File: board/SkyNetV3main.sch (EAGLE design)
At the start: 61 parts, among them IC1 HC_05, IC2 RF4463PRO, IC3 LPC1768, IC4 BCX17, IC5 TPS63001, IC6 MCP73871-2CCI/ML, Q1 32.768KHz, Q2 12MHz, Q3 IRLM6402, Q4 BSS138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

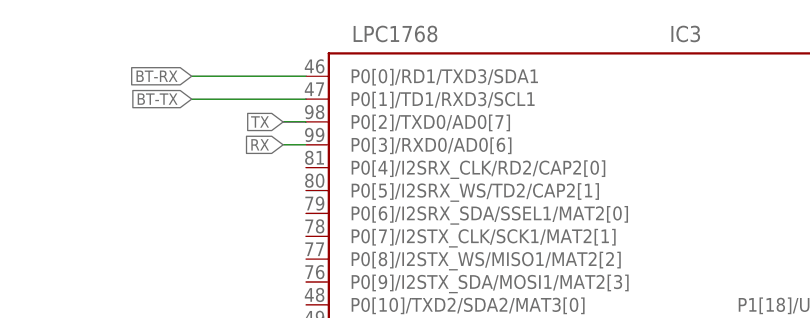
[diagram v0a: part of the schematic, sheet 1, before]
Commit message: corrected some distance problems and missing VALUEs
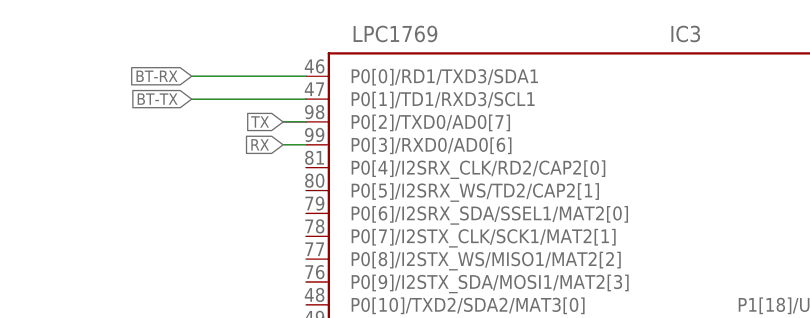
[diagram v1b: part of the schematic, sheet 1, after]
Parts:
- IC3: value LPC1768 -> LPC1769
- JP4: value (none) -> EXT
- SJ1: value (none) -> MEASURE
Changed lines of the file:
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@@
 </classes>
 <parts>
-<part name="IC3" library="lpc1xxx-v6" deviceset="LPC1768" device=""/>
+<part name="IC3" library="lpc1xxx-v6" deviceset="LPC1768" device="" value="LPC1769"/>
 <part name="IC1" library="Bluetooth HC-05" deviceset="HC_05" device=""/>
 <part name="FRAME1" library="frames" deviceset="A4L-LOC" device="" value="SkyNet Main"/>
@@
 <part name="GND31" library="supply1" deviceset="GND" device=""/>
 <part name="LED2" library="adafruit" deviceset="RGBLED" device="5050"/>
-<part name="SJ1" library="jumper" deviceset="SJ" device=""/>
+<part name="SJ1" library="jumper" deviceset="SJ" device="" value="MEASURE"/>
 <part name="SJ2" library="jumper" deviceset="SJ" device="" value="PROG"/>
 <part name="C12" library="microbuilder" deviceset="CAP_TANTALUM" device="C/6032_WAVE" value="100u"/>
@@
 <part name="GND19" library="supply1" deviceset="GND" device=""/>
 <part name="GND21" library="supply1" deviceset="GND" device=""/>
-<part name="JP4" library="skynet_other" deviceset="PIN-HEAD-1X3" device=""/>
+<part name="JP4" library="skynet_other" deviceset="PIN-HEAD-1X3" device="" value="EXT"/>
 <part name="FRAME4" library="frames" deviceset="A4L-LOC" device="" value="SkyNet Main"/>
 </parts>

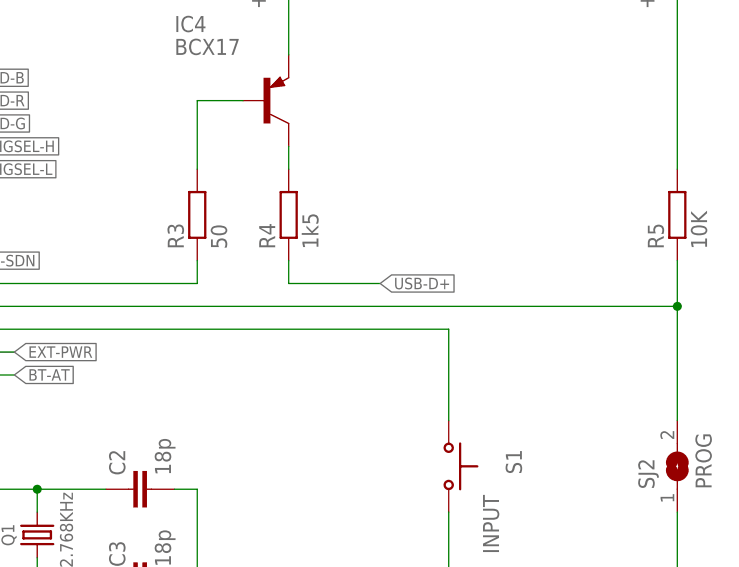
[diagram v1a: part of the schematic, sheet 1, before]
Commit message: layout & schematic fixes
+ layout: better ground flow
+ layout: more space for single parts
+ layout: marked GND on battery
+ layout: marked pinouts
+ schematics: fixed USB-connect->USB-plus connection
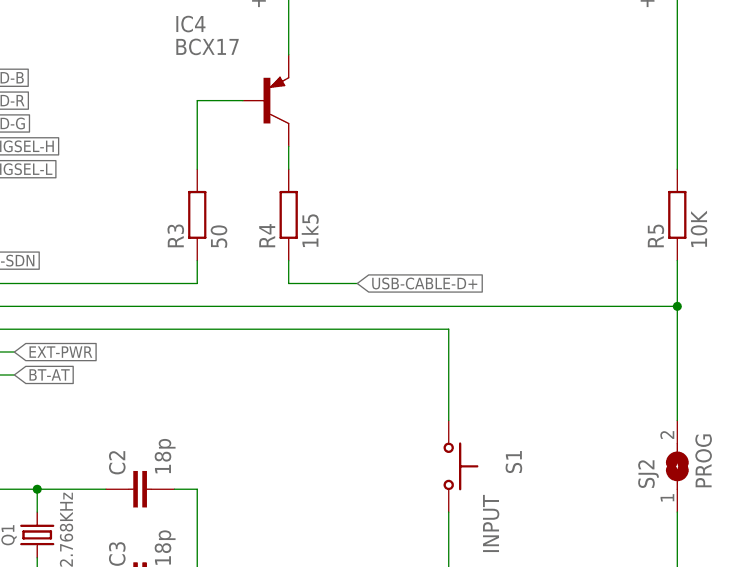
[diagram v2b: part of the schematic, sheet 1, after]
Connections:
- net N$2 renamed USB-CABLE-D-
- removed net N$3: R15.2, USB1.3
- new net USB-CABLE-D+: R15.2, R4.1, USB1.3
- net USB-D+: no longer R4.1
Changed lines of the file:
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@@
 <label x="68.58" y="99.06" size="1.27" layer="95" rot="MR0" xref="yes"/>
-</segment>
-<segment>
-<pinref part="R4" gate="G$1" pin="1"/>
-<wire x1="198.12" y1="81.28" x2="198.12" y2="78.74" width="0.1524" layer="91"/>
-<wire x1="198.12" y1="78.74" x2="208.28" y2="78.74" width="0.1524" layer="91"/>
-<label x="208.28" y="78.74" size="1.27" layer="95" xref="yes"/>
 </segment>
 </net>
@@
 <wire x1="71.12" y1="119.38" x2="68.58" y2="119.38" width="0.1524" layer="91"/>
 <label x="68.58" y="119.38" size="1.27" layer="95" rot="MR0" xref="yes"/>
+</segment>
+</net>
+<net name="USB-CABLE-D+" class="0">
+<segment>
+<pinref part="R4" gate="G$1" pin="1"/>
+<wire x1="198.12" y1="81.28" x2="198.12" y2="78.74" width="0.1524" layer="91"/>
+<wire x1="198.12" y1="78.74" x2="205.74" y2="78.74" width="0.1524" layer="91"/>
+<label x="205.74" y="78.74" size="1.27" layer="95" xref="yes"/>
 </segment>
 </net>
@@
 </segment>
 </net>
-<net name="N$2" class="0">
+<net name="USB-CABLE-D-" class="0">
 <segment>
 <pinref part="USB1" gate="G$1" pin="2"/>
@@
 </segment>
 </net>
-<net name="N$3" class="0">
+<net name="USB-CABLE-D+" class="0">
 <segment>
 <pinref part="R15" gate="G$1" pin="2"/>

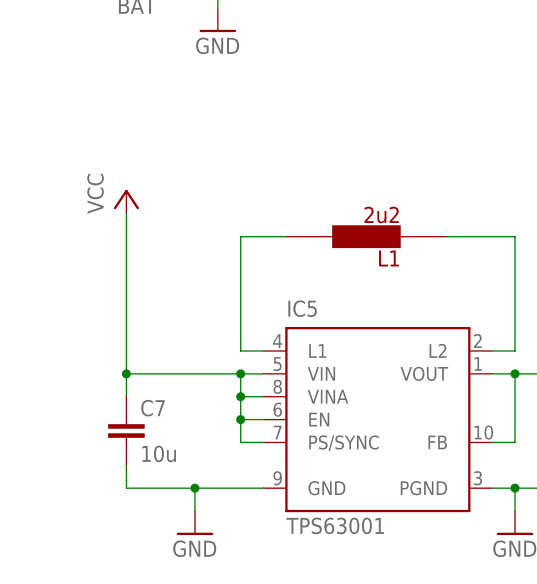
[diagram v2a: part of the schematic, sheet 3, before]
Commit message: board: connected PS/SYNC of buck boost converter
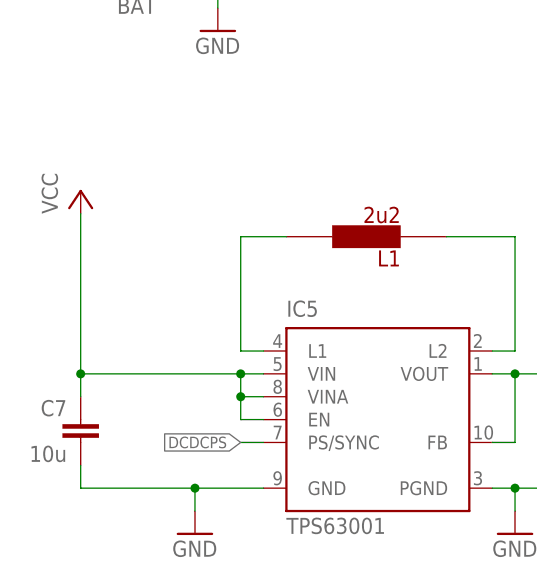
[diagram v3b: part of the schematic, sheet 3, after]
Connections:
- new net DCDCPS: IC3.P0[9]/I2STX_SDA/MOSI1/MAT2[3], IC5G$1.PS/SYNC
- net VCC: no longer IC5G$1.PS/SYNC
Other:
- moved on the sheet: C7
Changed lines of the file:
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@@
+</segment>
+</net>
+<net name="DCDCPS" class="0">
+<segment>
+<pinref part="IC3" gate="G$1" pin="P0[9]/I2STX_SDA/MOSI1/MAT2[3]"/>
+<wire x1="71.12" y1="142.24" x2="68.58" y2="142.24" width="0.1524" layer="91"/>
+<label x="68.58" y="142.24" size="1.27" layer="95" rot="MR0" xref="yes"/>
 </segment>
 </net>
@@
 <instance part="FRAME3" gate="G$1" x="0" y="0"/>
 <instance part="IC5" gate="G$1" x="48.26" y="22.86"/>
-<instance part="P+14" gate="VCC" x="20.32" y="48.26"/>
+<instance part="P+14" gate="VCC" x="15.24" y="48.26"/>
 <instance part="+3V8" gate="G$1" x="73.66" y="48.26"/>
 <instance part="C8" gate="G$1" x="73.66" y="22.86"/>
 <instance part="GND28" gate="1" x="63.5" y="10.16"/>
 <instance part="GND29" gate="1" x="27.94" y="10.16"/>
-<instance part="C7" gate="G$1" x="20.32" y="22.86"/>
+<instance part="C7" gate="G$1" x="15.24" y="22.86" rot="MR0"/>
 <instance part="P+15" gate="1" x="58.42" y="116.84"/>
 <instance part="BAT+5" gate="1" x="187.96" y="101.6"/>
@@
 <wire x1="35.56" y1="27.94" x2="33.02" y2="27.94" width="0.1524" layer="91"/>
 <pinref part="P+14" gate="VCC" pin="VCC"/>
-<wire x1="33.02" y1="27.94" x2="20.32" y2="27.94" width="0.1524" layer="91"/>
-<wire x1="20.32" y1="27.94" x2="20.32" y2="45.72" width="0.1524" layer="91"/>
+<wire x1="33.02" y1="27.94" x2="15.24" y2="27.94" width="0.1524" layer="91"/>
+<wire x1="15.24" y1="27.94" x2="15.24" y2="45.72" width="0.1524" layer="91"/>
 <pinref part="C7" gate="G$1" pin="1"/>
-<wire x1="20.32" y1="25.4" x2="20.32" y2="27.94" width="0.1524" layer="91"/>
-<junction x="20.32" y="27.94"/>
+<wire x1="15.24" y1="25.4" x2="15.24" y2="27.94" width="0.1524" layer="91"/>
+<junction x="15.24" y="27.94"/>
 <pinref part="IC5" gate="G$1" pin="VINA"/>
 <wire x1="35.56" y1="25.4" x2="33.02" y2="25.4" width="0.1524" layer="91"/>
@@
 <wire x1="33.02" y1="22.86" x2="33.02" y2="25.4" width="0.1524" layer="91"/>
 <junction x="33.02" y="25.4"/>
-<pinref part="IC5" gate="G$1" pin="PS/SYNC"/>
-<wire x1="35.56" y1="20.32" x2="33.02" y2="20.32" width="0.1524" layer="91"/>
-<wire x1="33.02" y1="20.32" x2="33.02" y2="22.86" width="0.1524" layer="91"/>
-<junction x="33.02" y="22.86"/>
 </segment>
 <segment>
@@
 <pinref part="IC5" gate="G$1" pin="GND"/>
 <wire x1="27.94" y1="15.24" x2="35.56" y2="15.24" width="0.1524" layer="91"/>
-<wire x1="27.94" y1="15.24" x2="20.32" y2="15.24" width="0.1524" layer="91"/>
+<wire x1="27.94" y1="15.24" x2="15.24" y2="15.24" width="0.1524" layer="91"/>
 <junction x="27.94" y="15.24"/>
 <pinref part="C7" gate="G$1" pin="2"/>
-<wire x1="20.32" y1="15.24" x2="20.32" y2="17.78" width="0.1524" layer="91"/>
+<wire x1="15.24" y1="15.24" x2="15.24" y2="17.78" width="0.1524" layer="91"/>
 </segment>
 <segment>
@@
 </segment>
 </net>
+<net name="DCDCPS" class="0">
+<segment>
+<pinref part="IC5" gate="G$1" pin="PS/SYNC"/>
+<wire x1="35.56" y1="20.32" x2="33.02" y2="20.32" width="0.1524" layer="91"/>
+<label x="33.02" y="20.32" size="1.27" layer="95" rot="MR0" xref="yes"/>
+</segment>
+</net>

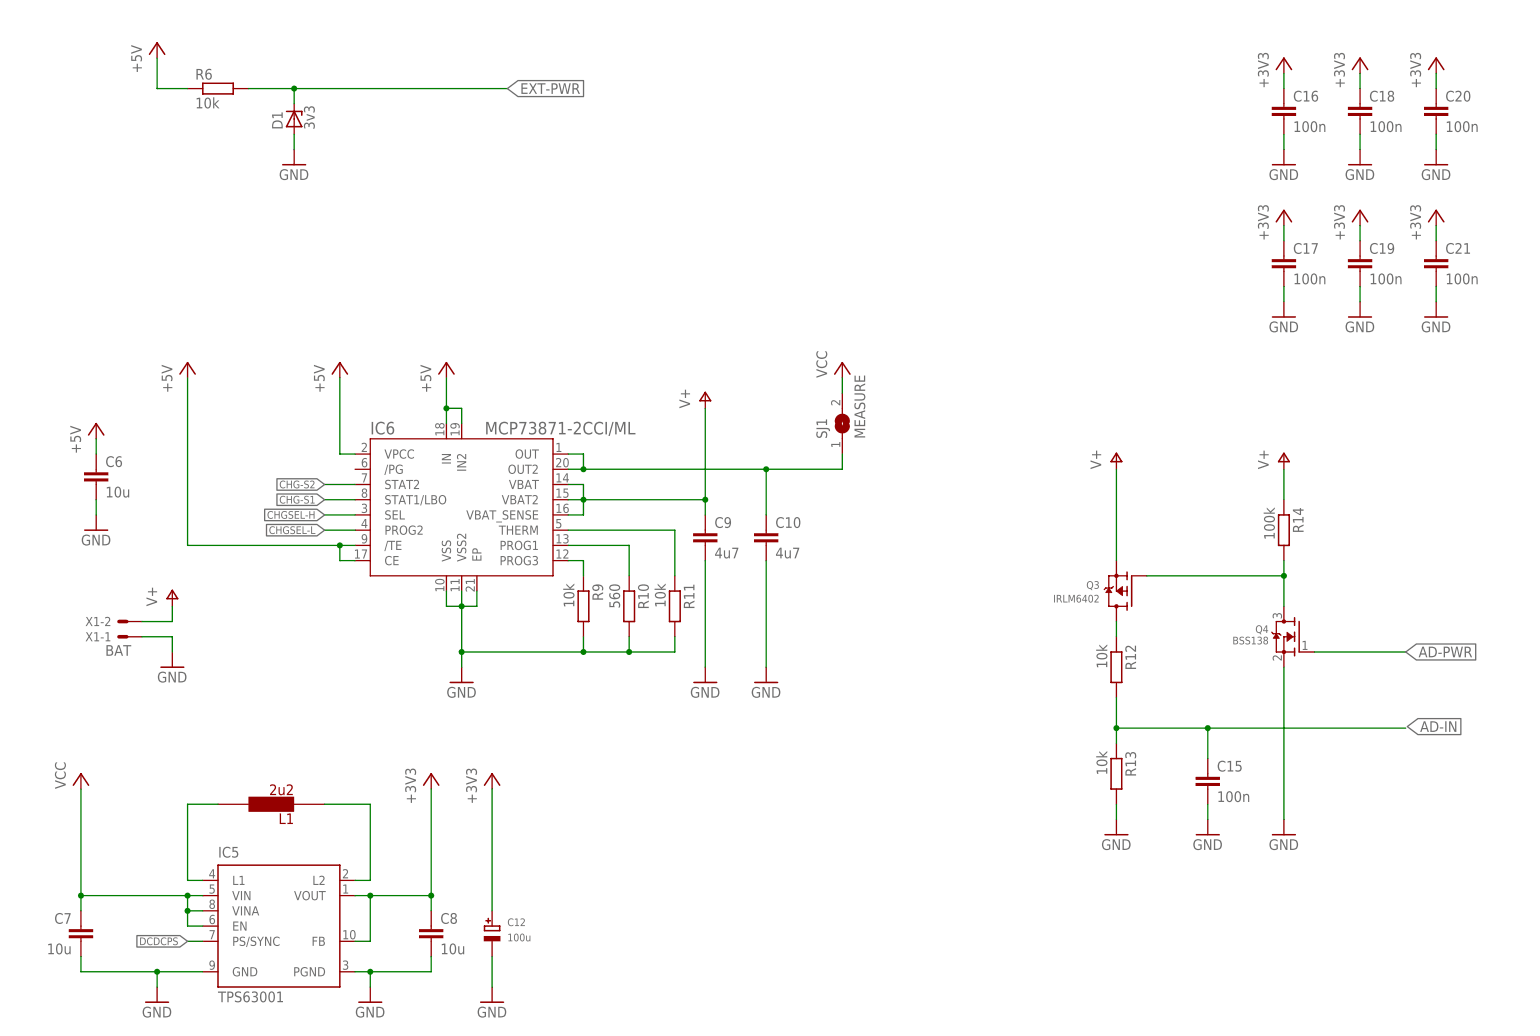
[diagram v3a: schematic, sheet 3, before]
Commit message: Schematic revised. TODO Radio remains
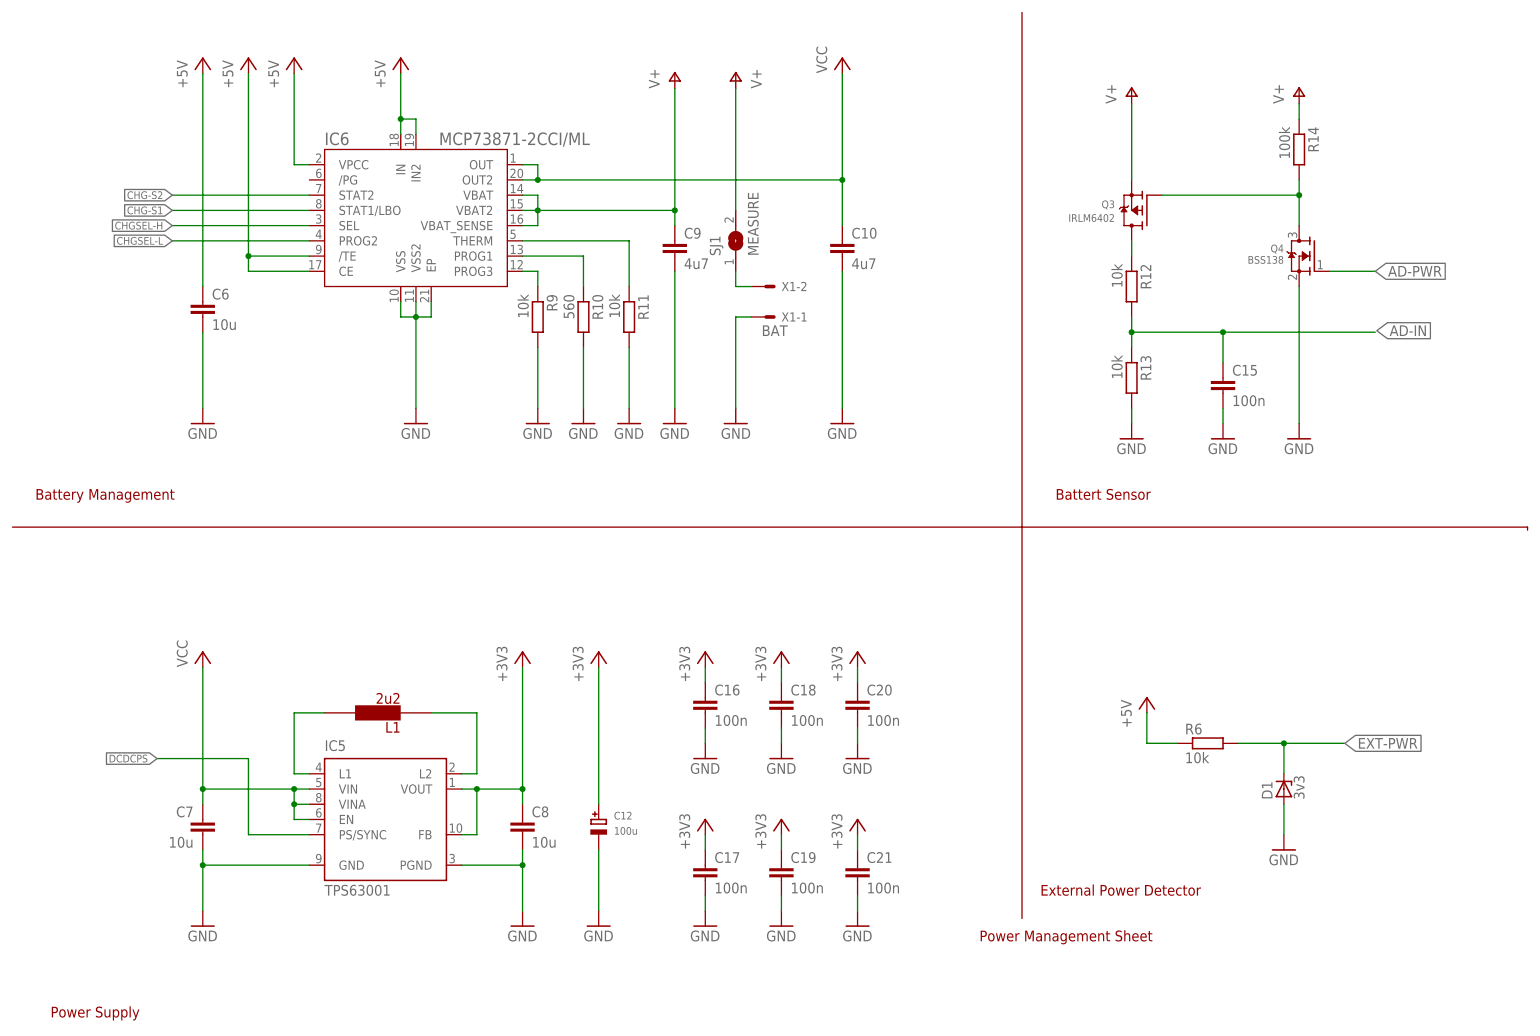
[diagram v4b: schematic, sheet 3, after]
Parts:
- removed U$1: ANT-MML, skynet_other:ANT-MML
- added X2: CONN-SMATHD, SteveMarple:CONN-SMATHD
- R3: value 50 -> 1k
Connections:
- removed net OUT2: C10.1, IC6.OUT, IC6.OUT2, SJ1.1
- new net BT-CN: IC1.PIO9, IC3.P0[10]/TXD2/SDA2/MAT3[0]
- new net N$2: SJ1.1, X1-2.S
- net ANT: now also X2.SIGNAL; no longer U$1.ANT
- net GND: now also IC1.GND1, IC1.GND2, X2.GND; no longer U$1.GND
- net V+: now also SJ1.2; no longer X1-2.S
- net VCC: now also C10.1, IC6.OUT, IC6.OUT2; no longer SJ1.2
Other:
- note added: "Addon"
- note added: "Battert Sensor"
- note added: "Battery Management"
- note added: "Controller Sheet"
- note added: "External Power Detector"
- note added: "JTAG"
- note added: "Power Management Sheet"
- note added: "Power Supply"
- note added: "Radio Sheet"
- note added: "Status LED"
- note added: "TODO: Connect GPIO1??"
- note added: "TODO: Mosfet for power control"
- note added: "USB"
- moved on the sheet: C10, C12, C13, C15, C16, C17, C18, C19, C20, C21, C22, C23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

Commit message: Schematic revised
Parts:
- removed X1: BAT, con-molex:22-23-2021
- added B1: PL503465, i7:1S
- added C14, C24: 10u, rcl:C-EUC1206K
- added Q5, Q6: IRLM6402, microbuilder:MOSFET-PWIDE
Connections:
- new net /BT-ON: IC3.P1[18]/USB_UP_LED/PWM1[1]/CAP1[0]
- new net /RF-ON: IC3.P1[19]/MCOA0/USB_PPWR/CAP1[1]
- new net N$3: Q5.G
- new net N$4: Q6.G
- new net VDD: C11.1, IC1.3V3, Q5.D
- new net VEE: C1.1, C13.+, IC2.VCC, Q6.D
- net +3V3: now also C14.1, Q5.S, Q6.S; no longer C1.1, C11.1, C13.+, IC1.3V3, IC2.VCC
- net GND: now also B1.P-, C14.2, C24.2; no longer X1-1.S
- net N$2: now also B1.P+; no longer X1-2.S
- net VCC: now also C24.1
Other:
- note added: "Bluetooth"
- note added: "Sub-GHz"
- note removed: "TODO: Connect GPIO1??"
- note removed: "TODO: Mosfet for power control"
- moved on the sheet: C1, C11, C12, C13, C16, C17, C18, C19, C20, C21, IC1, IC2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

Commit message: psu done
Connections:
- removed net N$3: Q5.G
- removed net N$4: Q6.G
- net /BT-ON: now also Q5.G
- net /RF-ON: now also Q6.G
- net GND: now also IC5TH.TH
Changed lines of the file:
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@@
 <part name="C24" library="rcl" deviceset="C-EU" device="C1206K" value="10u"/>
 <part name="B1" library="i7" deviceset="1S" device="" value="PL503465"/>
+<part name="GND8" library="supply1" deviceset="GND" device=""/>
 </parts>
 <sheets>
@@
 </segment>
 </net>
-<net name="N$3" class="0">
+<net name="/BT-ON" class="0">
 <segment>
 <pinref part="Q5" gate="G$1" pin="G"/>
@@
 </segment>
 </net>
-<net name="N$4" class="0">
+<net name="/RF-ON" class="0">
 <segment>
 <pinref part="Q6" gate="G$1" pin="G"/>
@@
 <instance part="C24" gate="G$1" x="25.4" y="40.64" rot="MR0"/>
 <instance part="B1" gate="G$1" x="127" y="121.92"/>
+<instance part="IC5" gate="TH" x="48.26" y="27.94"/>
+<instance part="GND8" gate="1" x="43.18" y="22.86"/>
 </instances>
 <busses>
@@
 <pinref part="GND38" gate="1" pin="GND"/>
 </segment>
-</net>
+<segment>
+<pinref part="GND8" gate="1" pin="GND"/>
+<wire x1="43.18" y1="25.4" x2="43.18" y2="27.94" width="0.1524" layer="91"/>
+<pinref part="IC5" gate="TH" pin="TH"/>
+<wire x1="43.18" y1="27.94" x2="45.72" y2="27.94" width="0.1524" layer="91"/>
+</segment>
+</net>

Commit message: cpu moved
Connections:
- net /BT-ON: now also IC3.P1[0]/ENET_TXD0; no longer IC3.P1[18]/USB_UP_LED/PWM1[1]/CAP1[0]
- net /RF-ON: now also IC3.P0[9]/I2STX_SDA/MOSI1/MAT2[3]; no longer IC3.P1[19]/MCOA0/USB_PPWR/CAP1[1]
- net AD-PWR: now also IC3.P1[17]/ENET_MDIO; no longer IC3.P1[0]/ENET_TXD0
- net DCDCPS: now also IC3.P0[8]/I2STX_WS/MISO1/MAT2[2]; no longer IC3.P0[9]/I2STX_SDA/MOSI1/MAT2[3]
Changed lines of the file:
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@@
-</segment>
-</net>
-<net name="AD-PWR" class="0">
-<segment>
-<pinref part="IC3" gate="G$1" pin="P1[0]/ENET_TXD0"/>
-<wire x1="160.02" y1="165.1" x2="228.6" y2="165.1" width="0.1524" layer="91"/>
-<label x="228.6" y="165.1" size="1.27" layer="95" xref="yes"/>
 </segment>
 </net>
@@
 </segment>
 </net>
-<net name="DCDCPS" class="0">
-<segment>
-<pinref part="IC3" gate="G$1" pin="P0[9]/I2STX_SDA/MOSI1/MAT2[3]"/>
-<wire x1="71.12" y1="142.24" x2="45.72" y2="142.24" width="0.1524" layer="91"/>
-<label x="45.72" y="142.24" size="1.27" layer="95" rot="MR0" xref="yes"/>
-</segment>
-</net>
 <net name="BT-CN" class="0">
 <segment>
@@
 </segment>
 </net>
+<net name="DCDCPS" class="0">
+<segment>
+<pinref part="IC3" gate="G$1" pin="P0[8]/I2STX_WS/MISO1/MAT2[2]"/>
+<wire x1="71.12" y1="144.78" x2="45.72" y2="144.78" width="0.1524" layer="91"/>
+<label x="45.72" y="144.78" size="1.778" layer="95" rot="R180" xref="yes"/>
+</segment>
+</net>
 <net name="/RF-ON" class="0">
 <segment>
-<pinref part="IC3" gate="G$1" pin="P1[19]/MCOA0/USB_PPWR/CAP1[1]"/>
-<wire x1="160.02" y1="137.16" x2="223.52" y2="137.16" width="0.1524" layer="91"/>
-<label x="223.52" y="137.16" size="1.778" layer="95" xref="yes"/>
+<pinref part="IC3" gate="G$1" pin="P0[9]/I2STX_SDA/MOSI1/MAT2[3]"/>
+<wire x1="71.12" y1="142.24" x2="43.18" y2="142.24" width="0.1524" layer="91"/>
+<label x="43.18" y="142.24" size="1.778" layer="95" rot="R180" xref="yes"/>
 </segment>
 </net>
 <net name="/BT-ON" class="0">
 <segment>
-<pinref part="IC3" gate="G$1" pin="P1[18]/USB_UP_LED/PWM1[1]/CAP1[0]"/>
-<wire x1="160.02" y1="139.7" x2="223.52" y2="139.7" width="0.1524" layer="91"/>
-<label x="223.52" y="139.7" size="1.778" layer="95" xref="yes"/>
+<pinref part="IC3" gate="G$1" pin="P1[0]/ENET_TXD0"/>
+<wire x1="160.02" y1="165.1" x2="228.6" y2="165.1" width="0.1524" layer="91"/>
+<label x="228.6" y="165.1" size="1.27" layer="95" xref="yes"/>
+</segment>
+</net>
+<net name="AD-PWR" class="0">
+<segment>
+<pinref part="IC3" gate="G$1" pin="P1[17]/ENET_MDIO"/>
+<wire x1="160.02" y1="142.24" x2="228.6" y2="142.24" width="0.1524" layer="91"/>
+<label x="228.6" y="142.24" size="1.778" layer="95" xref="yes"/>
 </segment>
 </net>
@@
 </sheet>
 </sheets>
-<errors>
-</errors>
 </schematic>
 </drawing>
